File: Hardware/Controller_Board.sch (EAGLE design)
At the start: 27 parts, among them Q7 3.6864MHz, U1 ATMEGA328P-PU, U2 REF3020AIDBZT

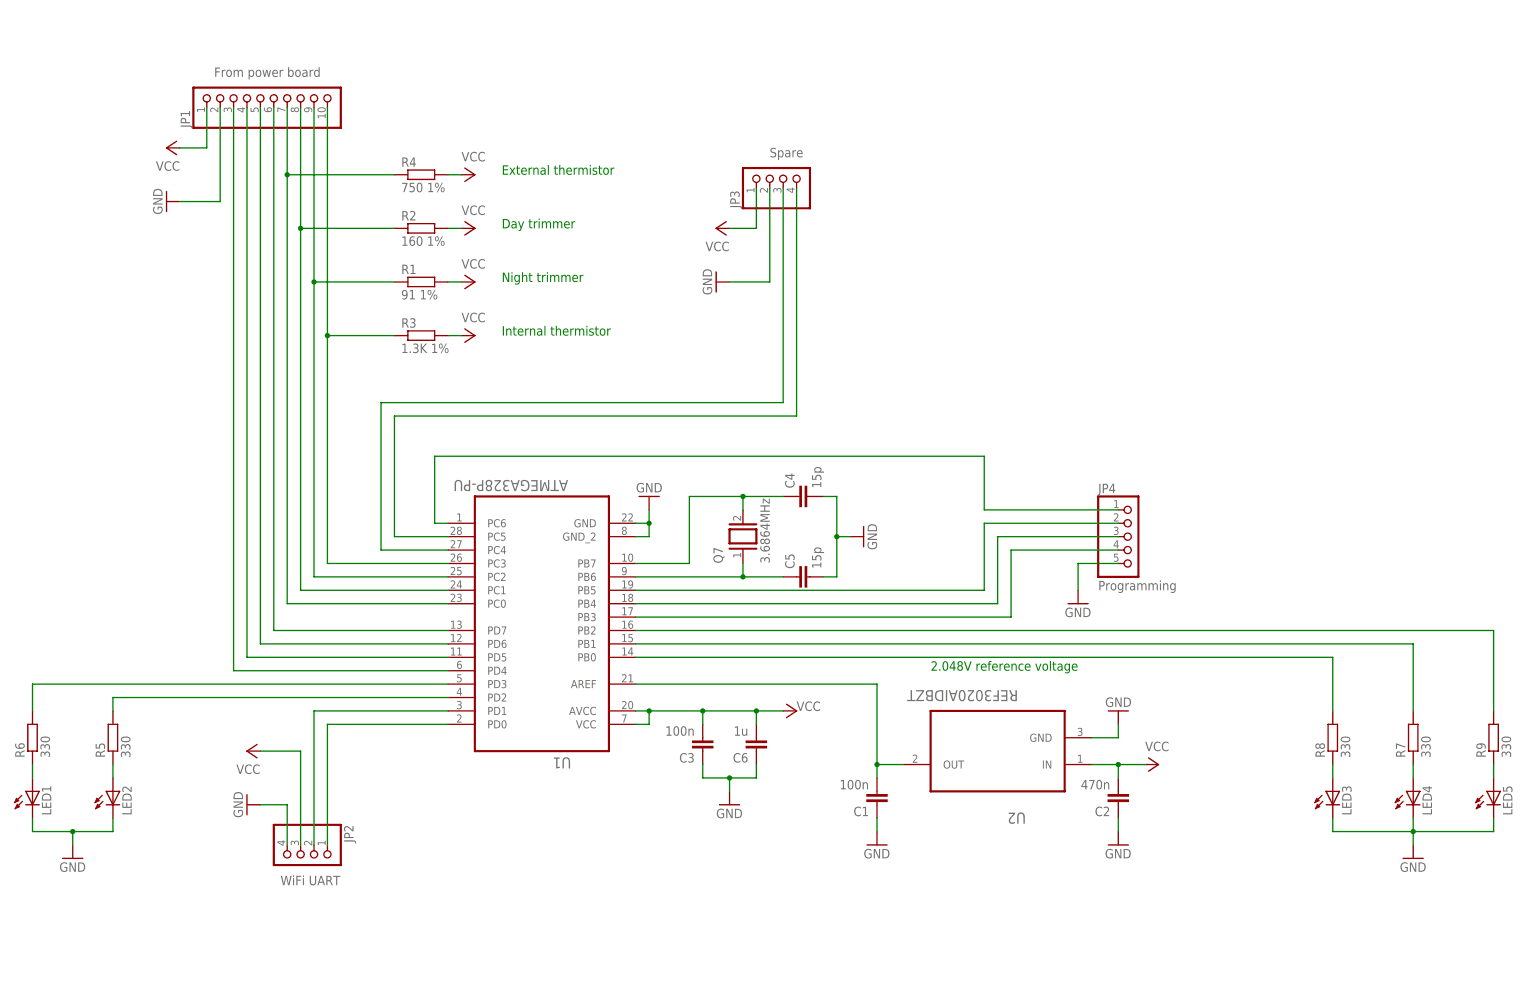
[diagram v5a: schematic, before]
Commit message: Changed controller board voltage dividers resistor values to allow a precision 3.3V reference voltage to be used. AC/DC 5V output voltage is not stable enough to grant precise measures.
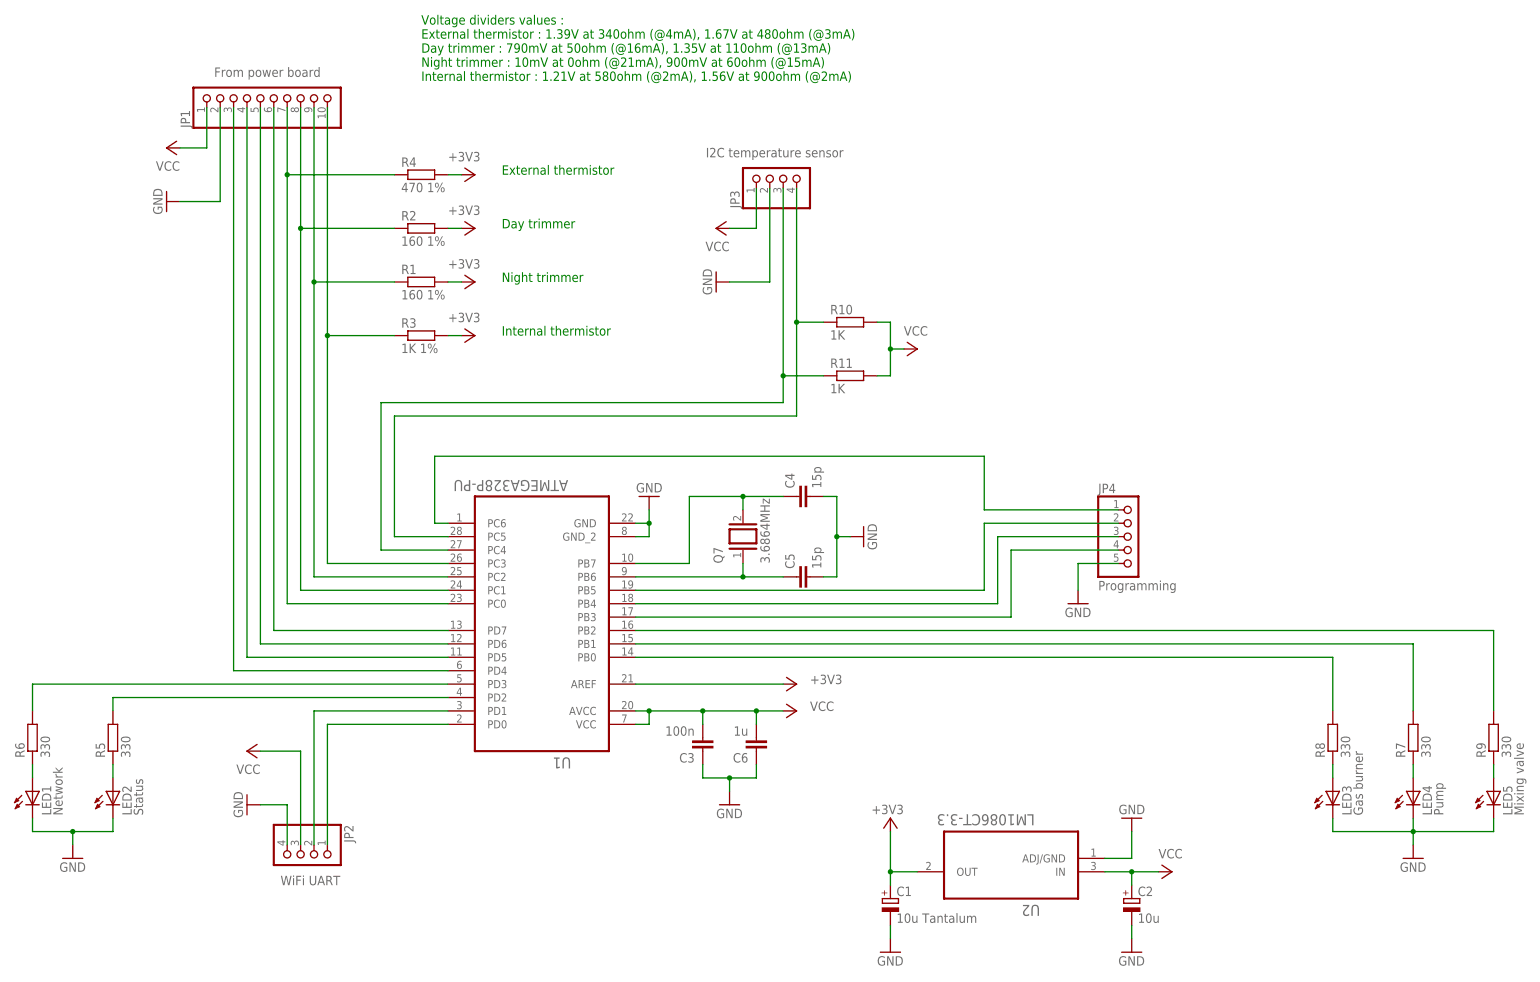
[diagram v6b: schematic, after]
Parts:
- added R10, R11: 1K, resistor:R-EU_0207/10
- C1: value 100n -> 10u Tantalum; device rcl:C-EU050-035X075 -> rcl:CPOL-EUE2.5-7
- C2: value 470n -> 10u; device rcl:C-EU050-035X075 -> rcl:CPOL-EUE2.5-7
- JP3: value Spare -> I2C temperature sensor
- LED1: value (none) -> Network
- LED2: value (none) -> Status
- LED3: value (none) -> Gas burner
- LED4: value (none) -> Pump
- LED5: value (none) -> Mixing valve
- R1: value 91 1% -> 160 1%
- R3: value 1.3K 1% -> 1K 1%
- R4: value 750 1% -> 470 1%
- U2: value REF3020AIDBZT -> LM1086CT-3.3; device REF3020AIDBZT:REF3020AIDBZT -> LM1086CT-3.3:LM1086CT-3.3
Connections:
- removed net N$16: C1.2, U1.AREF, U2.OUT
- new net +3V3: C1.+, R1.2, R2.2, R3.2, R4.2, U1.AREF, U2.OUT
- net GND: now also C1.-, C2.-, U2.ADJ/GND; no longer C1.1, C2.1, U2.GND
- net N$20: now also R11.1
- net N$23: now also R10.1
- net VCC: now also C2.+, R10.2, R11.2; no longer C2.2, R1.2, R2.2, R3.2, R4.2
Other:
- note added: "Voltage dividers values : External thermistor : 1.39V at 340ohm (@4mA), 1.67V at 480ohm (@3mA) Day trimmer : 790mV at 50ohm (@16mA), 1.35V at 110ohm (@13mA) Night trimmer : 10mV at 0ohm (@21mA), 900mV at 60ohm (@15mA) Internal thermistor : 1.21V at 580ohm (@2mA), 1.56V at 900ohm (@2mA)"
- note removed: "2.048V reference voltage"
- moved on the sheet: U2

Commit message: Added +3.3V and a GPIO to the controller board extension connector.
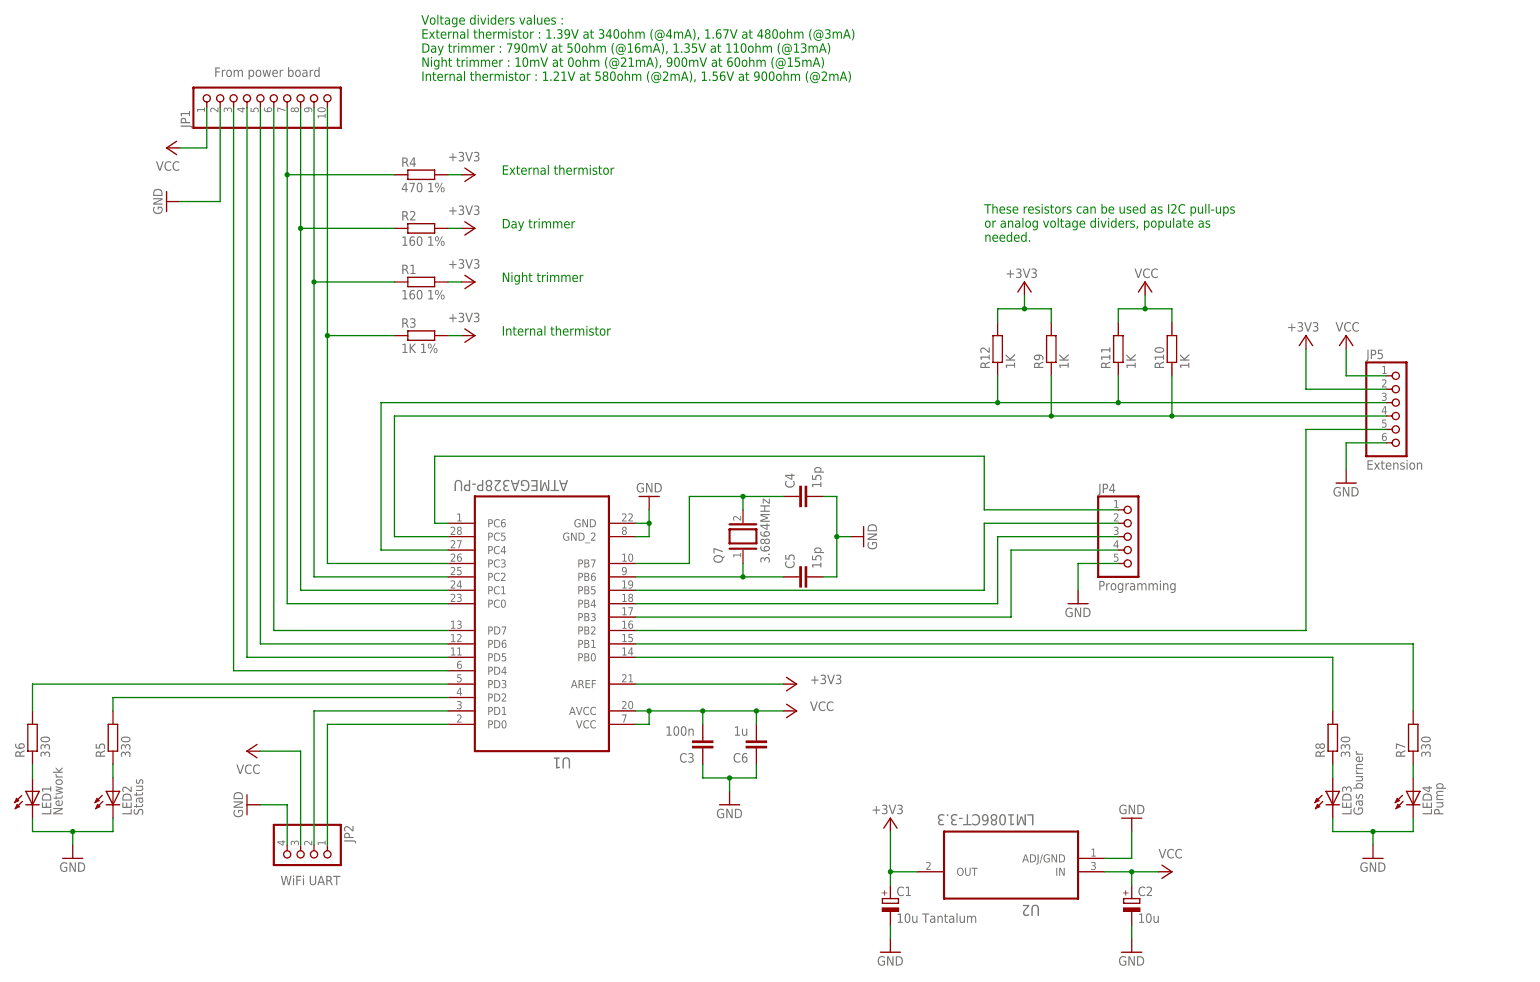
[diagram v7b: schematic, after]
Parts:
- removed JP3: I2C temperature sensor, pinhead:PINHD-1X4
- removed LED5: Mixing valve, led:LED5MM
- added JP5: Extension, pinhead:PINHD-1X6
- added R12: 1K, resistor:R-EU_0207/10
- R9: value 330 -> 1K
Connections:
- removed net N$28: R9.2, U1.PB2
- net +3V3: now also JP5.2, R12.2, R9.2
- net GND: now also JP5.6; no longer JP3.2, LED5.C
- net N$20: now also JP5.3, R12.1; no longer JP3.3
- net N$23: now also JP5.4, R9.1; no longer JP3.4
- net N$26: now also JP5.5, U1.PB2; no longer LED5.A, R9.1
- net VCC: now also JP5.1; no longer JP3.1
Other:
- note added: "These resistors can be used as I2C pull-ups or analog voltage dividers, populate as needed."
- moved on the sheet: R10, R11, R9
